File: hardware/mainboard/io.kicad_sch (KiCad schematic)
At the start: 39 parts, among them J2 MINI_DP_SINK, J3 DEBUG, J4 USB_C_Receptacle, Q10 BSS138, U12 TPD4E02B04DQA, U13 TPD4E02B04DQA, U14 CBTL02043A, U15 FUSB302B11MPX, U16 USB3318, X1 831056169

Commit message: Alternate DP connector
Signed-off-by: gatecat <gatecat@ds0.me>
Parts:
- J2: footprint meowality:E9320-001-01 -> meowality:2129320-3
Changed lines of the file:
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@@
     (property "Reference" "J2" (id 0) (at 45.6819 121.8143 0))
     (property "Value" "MINI_DP_SINK" (id 1) (at 45.6819 124.5894 0))
-    (property "Footprint" "meowality:E9320-001-01" (id 2) (at 43.18 177.8 0)
+    (property "Footprint" "meowality:2129320-3" (id 2) (at 43.18 177.8 0)
       (effects (font (size 1.27 1.27)) hide)
     )

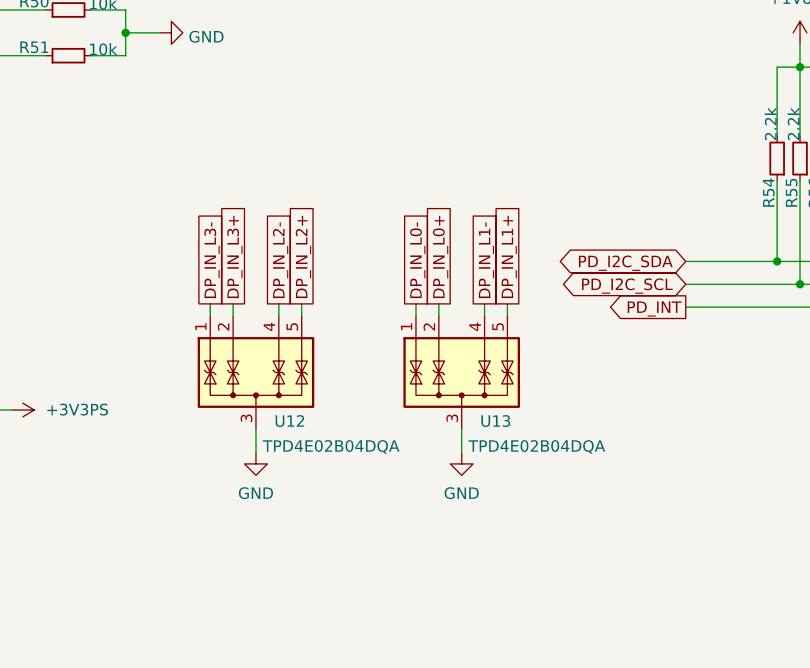
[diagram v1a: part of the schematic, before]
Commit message: Begin some routing
Signed-off-by: gatecat <gatecat@ds0.me>
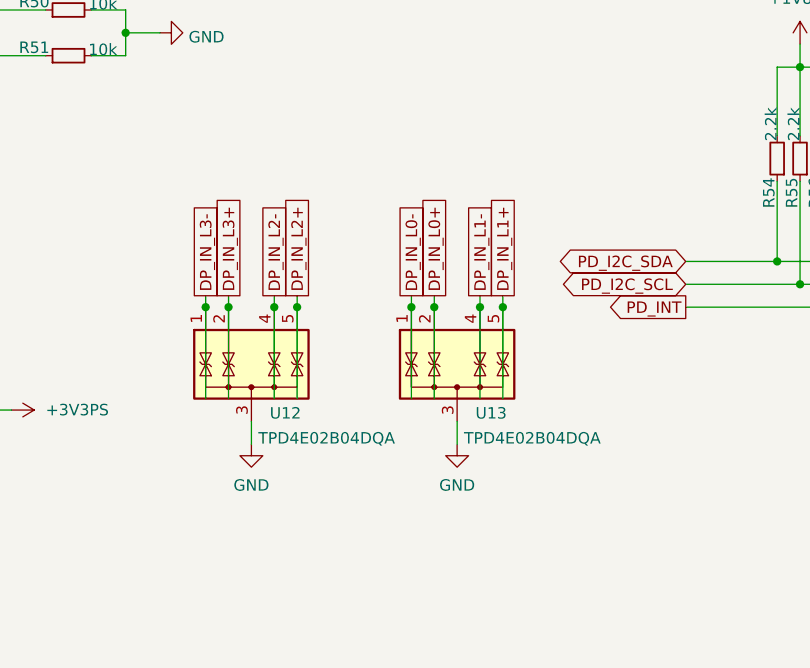
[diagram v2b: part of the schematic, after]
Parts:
- U12, U13: symbol Power_Protection:TPD4E02B04DQA -> meowality:TPD4E02B04DQA_thru
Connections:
- net DP_IN_L0+: now also U13.9 (NC)
- net DP_IN_L0-: now also U13.10 (NC)
- net DP_IN_L1+: now also U13.6 (NC)
- net DP_IN_L1-: now also U13.7 (NC)
- net DP_IN_L2+: now also U12.6 (NC)
- net DP_IN_L2-: now also U12.7 (NC)
- net DP_IN_L3+: now also U12.9 (NC)
- net DP_IN_L3-: now also U12.10 (NC)
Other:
- moved on the sheet: U12, U13

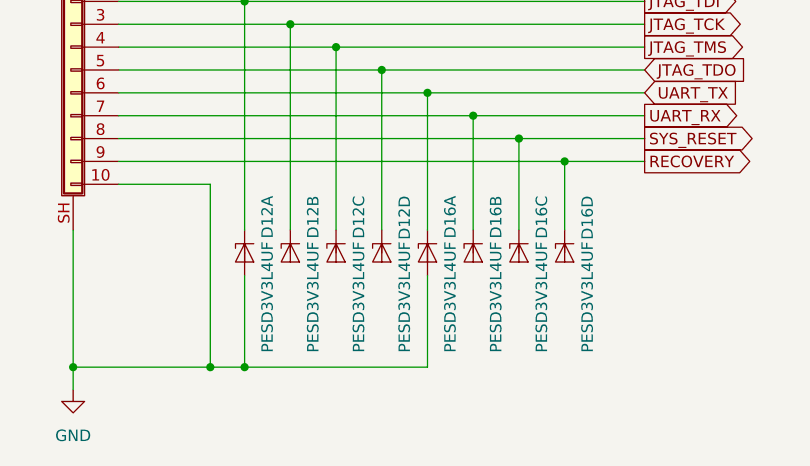
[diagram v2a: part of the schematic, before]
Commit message: Debug signal pinswaps and routing
Signed-off-by: gatecat <gatecat@ds0.me>
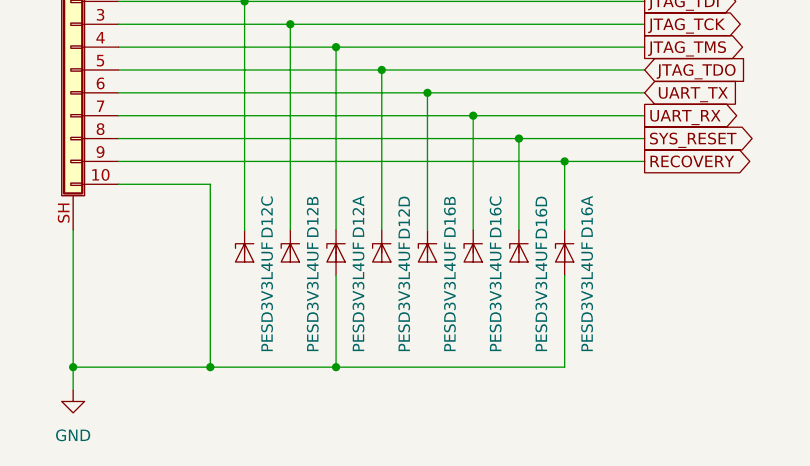
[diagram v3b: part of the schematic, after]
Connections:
- net JTAG_TDI: now also D12.4 (K3); no longer D12.1 (K1)
- net JTAG_TMS: now also D12.1 (K1); no longer D12.4 (K3)
- net RECOVERY: now also D16.1 (K1); no longer D16.6 (K4)
- net SYS_RESET: now also D16.6 (K4); no longer D16.4 (K3)
- net UART_RX: now also D16.4 (K3); no longer D16.3 (K2)
- net UART_TX: now also D16.3 (K2); no longer D16.1 (K1)
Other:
- moved on the sheet: D12A, D12C, D16A, D16B, D16C, D16D

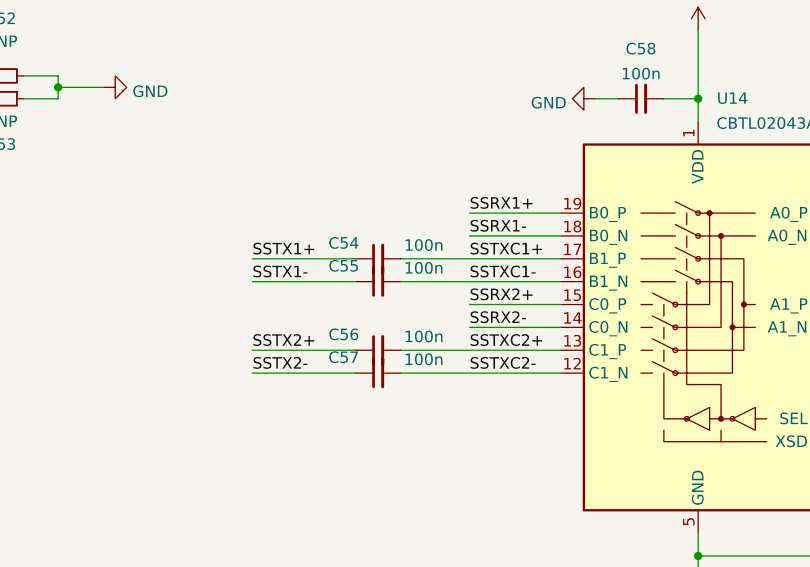
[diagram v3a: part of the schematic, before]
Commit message: USB and other misc routing
Signed-off-by: gatecat <gatecat@ds0.me>
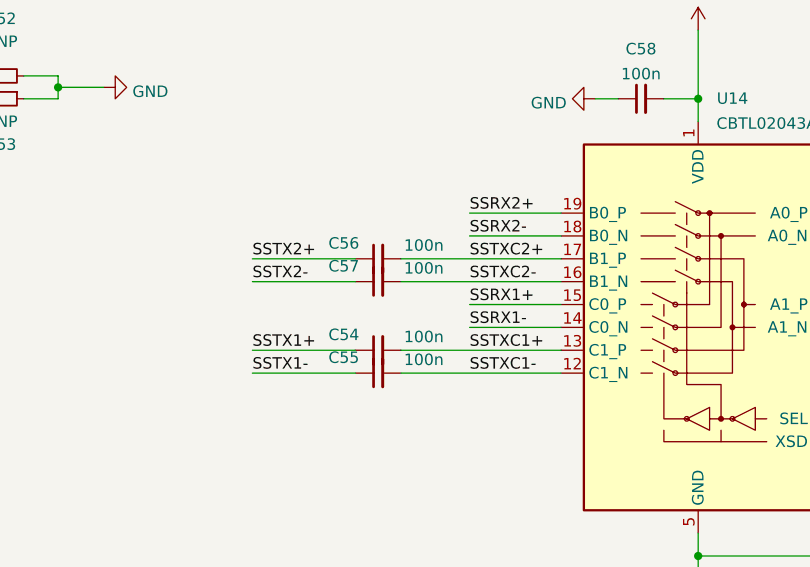
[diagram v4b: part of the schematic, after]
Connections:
- net SSRX1+: now also U14.15 (C0_P); no longer U14.19 (B0_P)
- net SSRX1-: now also U14.14 (C0_N); no longer U14.18 (B0_N)
- net SSRX2+: now also U14.19 (B0_P); no longer U14.15 (C0_P)
- net SSRX2-: now also U14.18 (B0_N); no longer U14.14 (C0_N)
- net SSTXC1+: now also U14.13 (C1_P); no longer U14.17 (B1_P)
- net SSTXC1-: now also U14.12 (C1_N); no longer U14.16 (B1_N)
- net SSTXC2+: now also U14.17 (B1_P); no longer U14.13 (C1_P)
- net SSTXC2-: now also U14.16 (B1_N); no longer U14.12 (C1_N)
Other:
- moved on the sheet: C54, C55, C56, C57
